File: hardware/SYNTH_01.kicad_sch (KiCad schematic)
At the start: 6 parts, among them J1 RPI4_GPIO_40, K1 SW_Push, U1 MCP23017-E/SP

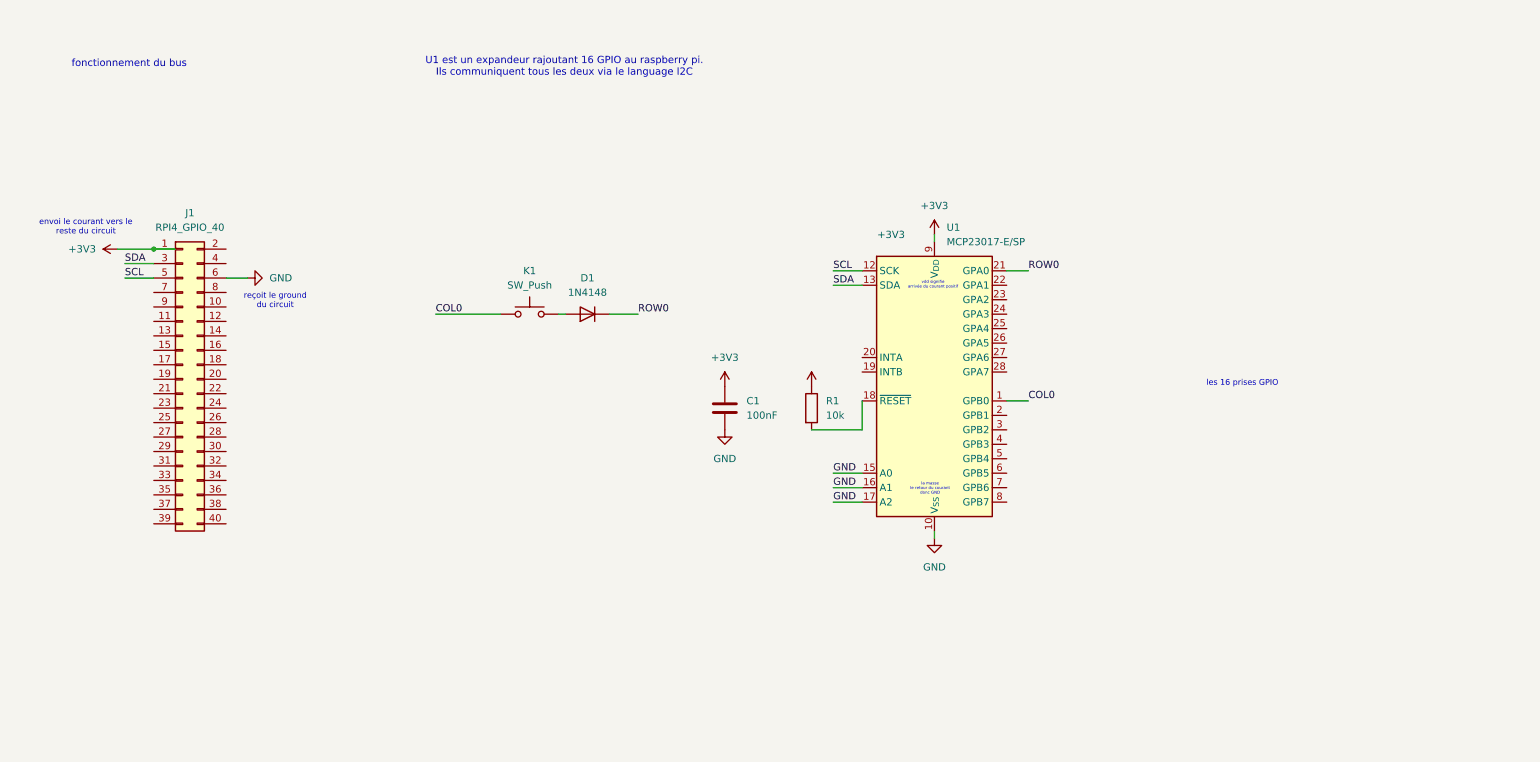
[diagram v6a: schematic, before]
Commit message: [PCB] testing matrix with 2x5 layout
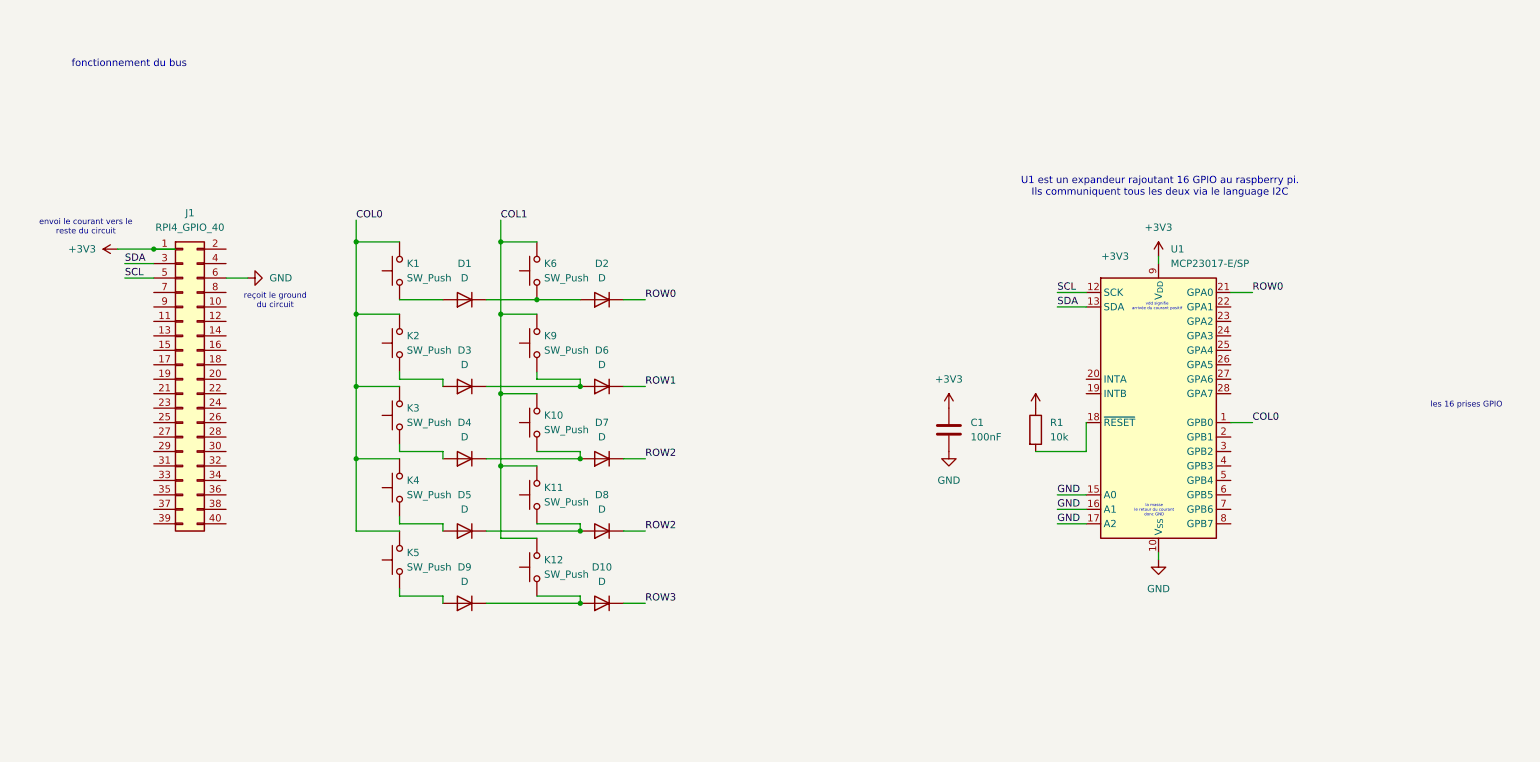
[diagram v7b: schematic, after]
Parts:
- added D10, D2, D3, D4, D5, D6, D7, D8, D9: D, symbol Device:D
- added K10, K11, K12, K2, K3, K4, K5, K6, K9: SW_Push, symbol Switch:SW_Push
- D1: value 1N4148 -> D
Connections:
- net COL0: now also K1.2, K2.2, K3.2, K4.2, K5.2; no longer K1.1
- net ROW0: now also D2.1 (K); no longer D1.1 (K)
- net at D1.2 (A): now also K1.1; no longer K1.2
- new net: D5.1 (K), D8.2 (A), K11.1
- new net: D5.2 (A), K4.1
- new net: D10.2 (A), D9.1 (K), K12.1
- new net: D4.1 (K), D7.2 (A), K10.1
- new net: D9.2 (A), K5.1
- new net: D3.2 (A), K2.1
- new net: D3.1 (K), D6.2 (A), K9.1
- new net: D1.1 (K), D2.2 (A), K6.1
- new net: D4.2 (A), K3.1
- new net COL1: K10.2, K11.2, K12.2, K6.2, K9.2
- new net ROW1: D6.1 (K)
- new net ROW2: D7.1 (K), D8.1 (K)
- new net ROW3: D10.1 (K)
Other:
- moved on the sheet: C1, K1, R1, U1

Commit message: [PCB] fixed diode branching
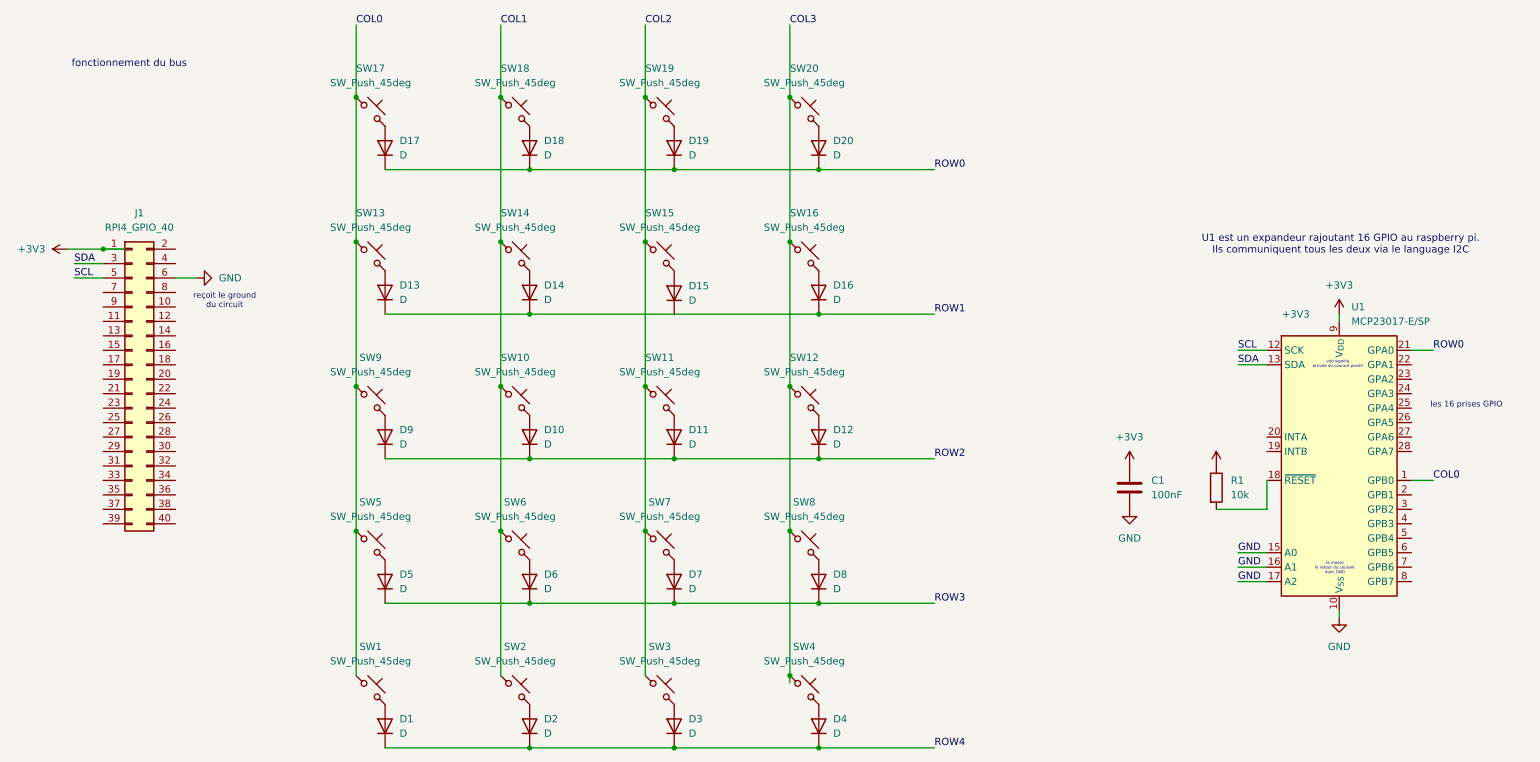
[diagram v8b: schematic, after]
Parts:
- removed K1, K10, K11, K12, K2, K3, K4, K5, K6, K9: SW_Push, symbol Switch:SW_Push
- added D11, D12, D13, D14, D15, D16, D17, D18, D19, D20: D, symbol Device:D
- added SW1, SW10, SW11, SW12, SW13, SW14, SW15, SW16, SW17, SW18, SW19, SW2, SW20, SW3, SW4, SW5, SW6, SW7, SW8, SW9: SW_Push_45deg, symbol Switch:SW_Push_45deg
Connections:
- net COL0: now also SW1.1, SW13.1, SW17.1, SW5.1, SW9.1
- net COL1: now also SW10.1, SW14.1, SW18.1, SW2.1, SW6.1
- net ROW0: now also D17.1 (K), D18.1 (K), D19.1 (K), D20.1 (K); no longer D2.1 (K)
- net ROW1: now also D13.1 (K), D14.1 (K), D16.1 (K); no longer D6.1 (K)
- net ROW2: now also D10.1 (K), D9.1 (K), D11.1 (K), D12.1 (K); no longer D7.1 (K), D8.1 (K)
- net ROW3: now also D5.1 (K), D6.1 (K), D7.1 (K), D8.1 (K); no longer D10.1 (K)
- net at D8.2 (A): now also SW8.2; no longer D5.1 (K)
- net at D5.2 (A): now also SW5.2
- net at D10.2 (A): now also SW10.2; no longer D9.1 (K)
- net at D7.2 (A): now also SW7.2; no longer D4.1 (K)
- net at D9.2 (A): now also SW9.2
- net at D3.2 (A): now also SW3.2
- net at D6.2 (A): now also SW6.2; no longer D3.1 (K)
- net at D2.2 (A): now also SW2.2; no longer D1.1 (K)
- net at D1.2 (A): now also SW1.2
- net at D4.2 (A): now also SW4.2
- new net: D17.2 (A), SW17.2
- new net: D20.2 (A), SW20.2
- new net: D13.2 (A), SW13.2
- new net: D11.2 (A), SW11.2
- new net: D19.2 (A), SW19.2
- new net: D14.2 (A), SW14.2
- new net: D12.2 (A), SW12.2
- new net: D18.2 (A), SW18.2
- new net: D16.2 (A), SW16.2
- new net COL2: SW11.1, SW15.1, SW19.1, SW3.1, SW7.1
- new net COL3: SW12.1, SW16.1, SW20.1, SW4.1, SW8.1
- new net ROW4: D1.1 (K), D2.1 (K), D3.1 (K), D4.1 (K)
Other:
- note removed: "envoi le courant vers le reste du circuit"
- moved on the sheet: C1, J1, R1, U1
